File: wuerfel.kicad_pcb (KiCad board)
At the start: 2 copper layers, 50 x 30 mm, 26 parts, among them IC1 M74HC4060YRM13TR, J1 PINHD_1x2_Female, Q1 BC857, SW1 SW_Push

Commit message: Generated Gerber updated Readme
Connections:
- IC1 pad 11: Net-(IC1-~{[Oslash]I}) -> GND
- R4 pad 1: Net-(IC1-~{[Oslash]I}) -> GND
- SW1 pad 2: Net-(IC1-~{[Oslash]I}) -> GND
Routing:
- net Net-(IC1-~{[Oslash]I}): track 20.3 -> 0.00 mm
- net GND: track 45.3 -> 65.6 mm
- net +5V: track 84.1 -> 81.7 mm

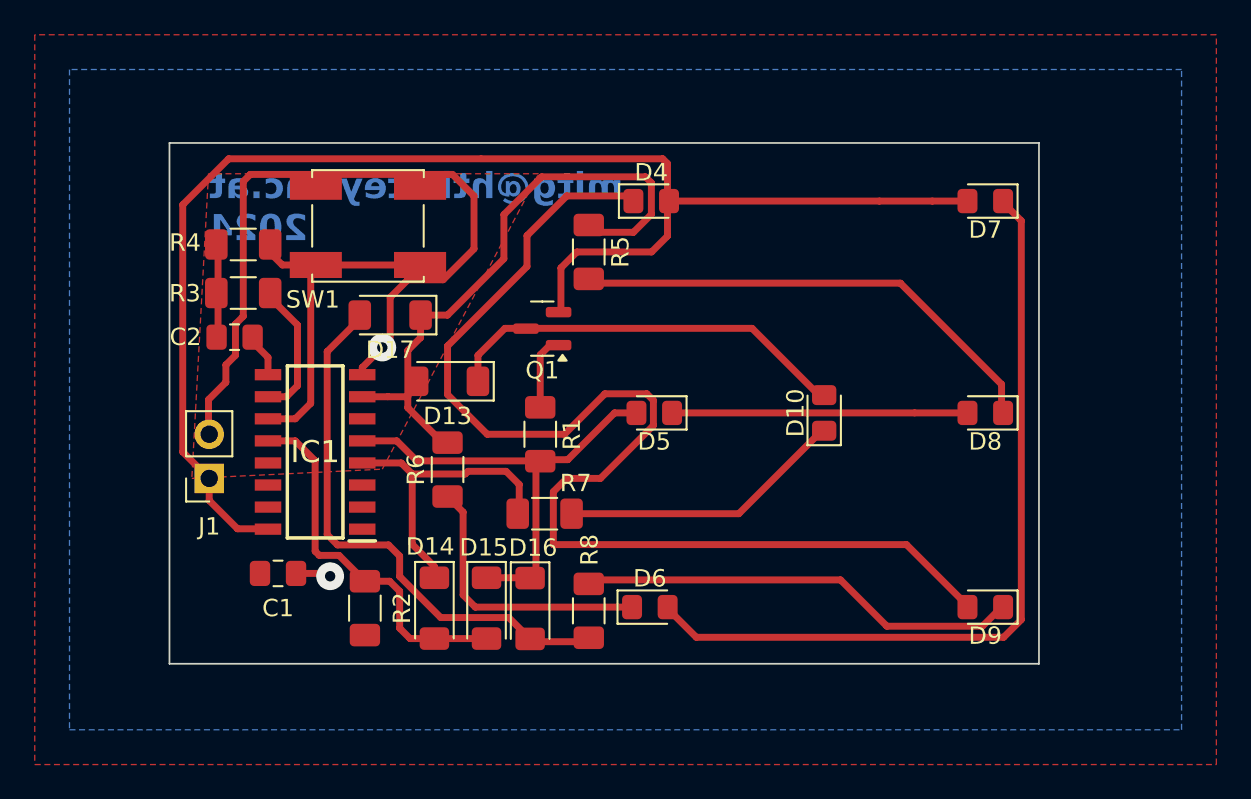
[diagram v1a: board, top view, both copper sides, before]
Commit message: Error at groundplane sw1
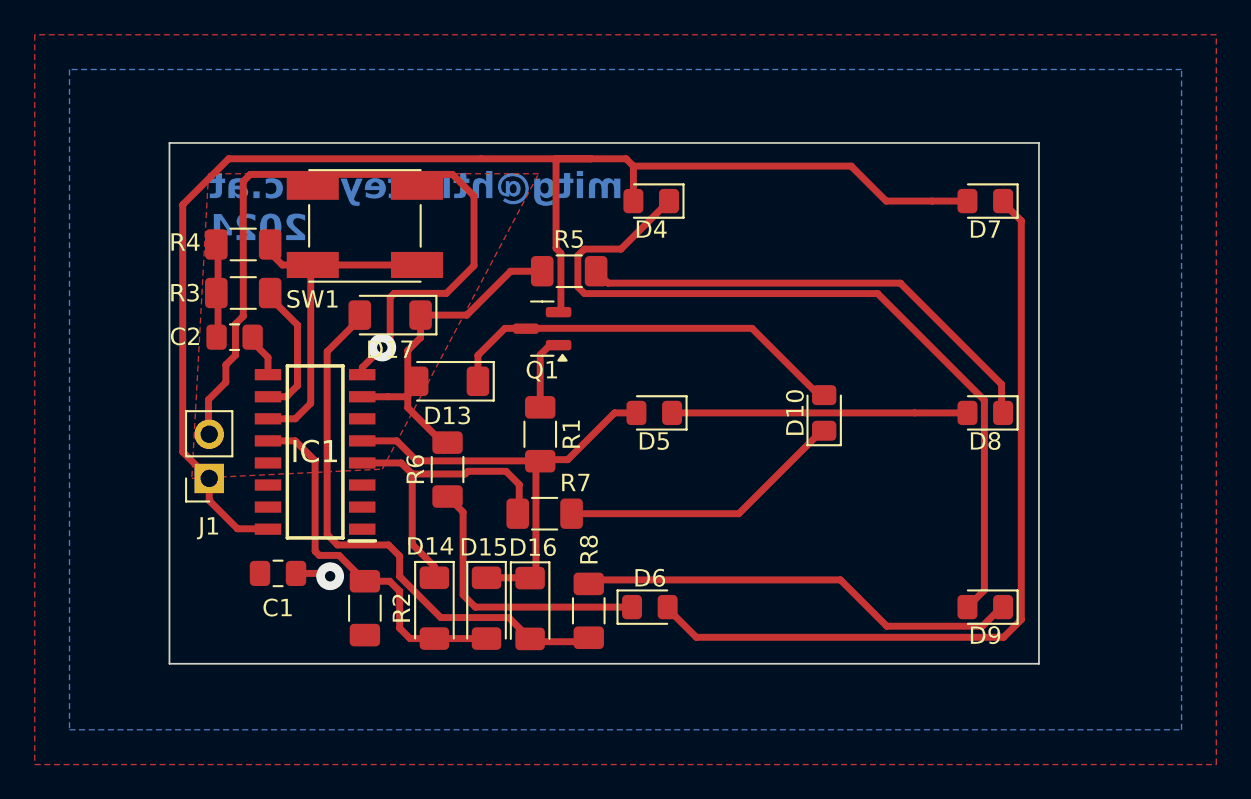
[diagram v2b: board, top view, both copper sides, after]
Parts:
- moved R5 1.58 mm to (213.8, 53.6), turned to 0 degrees
- moved SW1 0.18 mm to (202.0, 51.0)
- turned D4 to 180 degrees
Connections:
- IC1 pad 11: GND -> Net-(IC1-~{[Oslash]I})
- R4 pad 1: GND -> Net-(IC1-~{[Oslash]I})
- SW1 pad 2: GND -> Net-(IC1-~{[Oslash]I})
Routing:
- net Net-(D4-K): track 69.5 -> 46.8 mm
- net Net-(IC1-~{[Oslash]I}): track 0.00 -> 20.3 mm
- net GND: track 65.6 -> 45.9 mm
- net Net-(D13-A): track 35.5 -> 19.5 mm

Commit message: cleanup add folder pics
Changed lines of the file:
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@@
 		(tags "LED handsolder")
 		(property "Reference" "D4"
-			(at 0 -1.65 180)
+			(at 0.002399 -1.903755 180)
 			(layer "F.SilkS")
 			(effects
@@
 		)
 		(fp_text user "${REFERENCE}"
-			(at 0 0 360)
+			(at 0 0 0)
 			(layer "F.Fab")
 			(effects
@@
 		(net_name "GND")
 		(layer "F.Cu")
-		(name "$teardrop_padvia$")
-		(hatch full 0.1)
-		(priority 30000)
-		(attr
-			(teardrop
-				(type padvia)
-			)
-		)
-		(connect_pads yes
-			(clearance 0)
+		(hatch edge 0.5)
+		(priority 2)
+		(connect_pads
+			(clearance 0.5)
 		)
-		(min_thickness 0.0254)
+		(min_thickness 0.25)
 		(filled_areas_thickness no)
 		(fill yes
 			(thermal_gap 0.5)
 			(thermal_bridge_width 0.5)
-			(island_removal_mode 1)
-			(island_area_min 10)
 		)
 		(polygon
 			(pts
-				(xy 198.432224 70.8) (xy 198.432224 71.2) (xy 199.693853 71.901104) (xy 200.001 71.162) (xy 199.693853 70.422896)
+				(xy 195 48) (xy 192 49) (xy 192.04 65.532) (xy 205 66) (xy 205 56) (xy 208 56) (xy 212 53) (xy 212 48)
 			)
 		)
 	)
 	(zone
-		(net 2)
-		(net_name "GND")
+		(net 1)
+		(net_name "+5V")
 		(layer "F.Cu")
 		(hatch edge 0.5)
-		(priority 2)
+		(priority 1)
 		(connect_pads
 			(clearance 0.5)
@@
 		(polygon
 			(pts
-				(xy 193 48) (xy 192.04 65.532) (xy 203 65) (xy 212 48)
+				(xy 183 40) (xy 183 82) (xy 251 82) (xy 251 40)
 			)
 		)
 	)
 	(zone
-		(net 1)
-		(net_name "+5V")
+		(net 2)
+		(net_name "GND")
 		(layer "F.Cu")
-		(hatch edge 0.5)
-		(priority 1)
-		(connect_pads
-			(clearance 0.5)
+		(name "$teardrop_padvia$")
+		(hatch full 0.1)
+		(priority 30000)
+		(attr
+			(teardrop
+				(type padvia)
+			)
 		)
-		(min_thickness 0.25)
+		(connect_pads yes
+			(clearance 0)
+		)
+		(min_thickness 0.0254)
 		(filled_areas_thickness no)
 		(fill yes
 			(thermal_gap 0.5)
 			(thermal_bridge_width 0.5)
+			(island_removal_mode 1)
+			(island_area_min 10)
 		)
 		(polygon
 			(pts
-				(xy 183 40) (xy 183 82) (xy 251 82) (xy 251 40)
+				(xy 198.432224 70.8) (xy 198.432224 71.2) (xy 199.693853 71.901104) (xy 200.001 71.162) (xy 199.693853 70.422896)
 			)
 		)
